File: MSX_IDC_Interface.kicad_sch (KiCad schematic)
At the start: 27 parts, among them J1 DE1 GPIO, J2 Conn_01x03_Male, J3 Conn_01x03_Male, J4 Conn_01x03_Male, J5 Conn_01x03_Male, J6 Conn_01x03_Male, J7 Conn_01x03_Male, Q1 2N2222, Q2 2N2222, U1 74LVC245A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

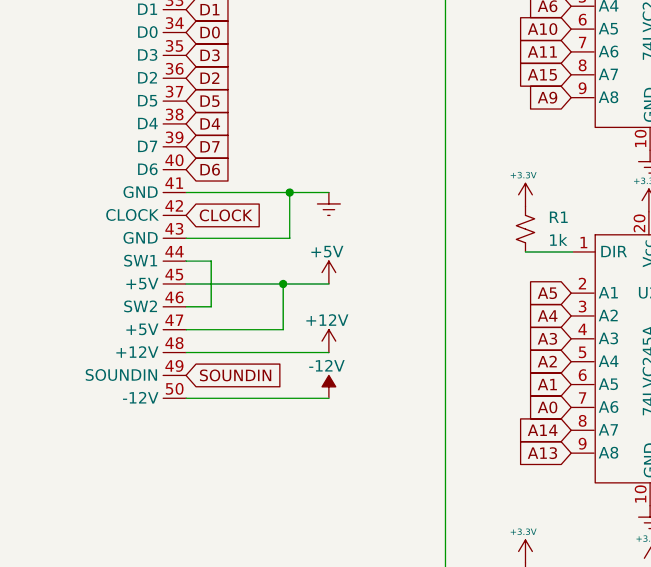
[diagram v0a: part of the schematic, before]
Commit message: Resolvig clearance issues - wip
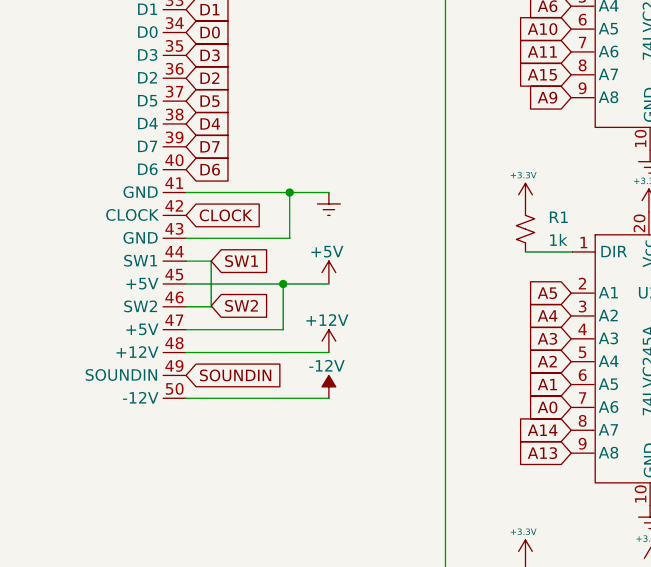
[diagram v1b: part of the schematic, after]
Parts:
- J2, J3, J4, J5, J6, J7: footprint Connector_PinHeader_1.00mm:PinHeader_1x03_P1.00mm_Vertical -> Connector_PinHeader_2.54mm:PinHeader_1x03_P2.54mm_Vertical
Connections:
- net SW1: now reaches CONN1.44 (SW1), CONN1.46 (SW2)
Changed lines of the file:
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@@
+    )
+  )
+  (global_label "SW1" (shape input) (at 35.1862 178.308 0) (fields_autoplaced)
+    (effects (font (size 1.27 1.27)) (justify left))
+    (property "Intersheet References" "${INTERSHEET_REFS}" (id 0) (at 41.4698 178.2286 0)
+      (effects (font (size 1.27 1.27)) (justify left) hide)
     )
   )
@@
     (property "Intersheet References" "${INTERSHEET_REFS}" (id 0) (at 65.6952 65.3574 0)
       (effects (font (size 1.27 1.27)) (justify right) hide)
+    )
+  )
+  (global_label "SW2" (shape input) (at 35.1862 183.2825 0) (fields_autoplaced)
+    (effects (font (size 1.27 1.27)) (justify left))
+    (property "Intersheet References" "${INTERSHEET_REFS}" (id 0) (at 41.4698 183.2031 0)
+      (effects (font (size 1.27 1.27)) (justify left) hide)
     )
   )
@@
   (symbol (lib_id "power:GNDREF") (at 109.5184 219.583 0) (unit 1)
     (in_bom yes) (on_board yes) (fields_autoplaced)
-    (property "Reference" "#PWR?" (id 0) (at 109.5184 225.933 0)
+    (property "Reference" "#PWR0104" (id 0) (at 109.5184 225.933 0)
       (effects (font (size 1.27 1.27)) hide)
     )
@@
   (symbol (lib_id "power:GNDREF") (at 108.204 100.203 0) (unit 1)
     (in_bom yes) (on_board yes) (fields_autoplaced)
-    (property "Reference" "#PWR?" (id 0) (at 108.204 106.553 0)
+    (property "Reference" "#PWR0105" (id 0) (at 108.204 106.553 0)
       (effects (font (size 1.27 1.27)) hide)
     )
@@
   (symbol (lib_id "power:GNDREF") (at 108.204 60.706 0) (unit 1)
     (in_bom yes) (on_board yes) (fields_autoplaced)
-    (property "Reference" "#PWR?" (id 0) (at 108.204 67.056 0)
+    (property "Reference" "#PWR0106" (id 0) (at 108.204 67.056 0)
       (effects (font (size 1.27 1.27)) hide)
     )
@@
       (effects (font (size 1.27 1.27)) hide)
     )
-    (property "Footprint" "Connector_PinHeader_1.00mm:PinHeader_1x03_P1.00mm_Vertical" (id 2) (at 51.816 118.364 0)
+    (property "Footprint" "Connector_PinHeader_2.54mm:PinHeader_1x03_P2.54mm_Vertical" (id 2) (at 51.816 118.364 0)
       (effects (font (size 1.27 1.27)) hide)
     )
@@
       (effects (font (size 1.27 1.27)) hide)
     )
-    (property "Footprint" "Connector_PinHeader_1.00mm:PinHeader_1x03_P1.00mm_Vertical" (id 2) (at 103.124 97.663 0)
+    (property "Footprint" "Connector_PinHeader_2.54mm:PinHeader_1x03_P2.54mm_Vertical" (id 2) (at 103.124 97.663 0)
       (effects (font (size 1.27 1.27)) hide)
     )
@@
       (effects (font (size 1.27 1.27)) hide)
     )
-    (property "Footprint" "Connector_PinHeader_1.00mm:PinHeader_1x03_P1.00mm_Vertical" (id 2) (at 103.124 58.166 0)
+    (property "Footprint" "Connector_PinHeader_2.54mm:PinHeader_1x03_P2.54mm_Vertical" (id 2) (at 103.124 58.166 0)
       (effects (font (size 1.27 1.27)) hide)
     )
@@
   (symbol (lib_id "power:GNDREF") (at 108.847 140.2388 0) (unit 1)
     (in_bom yes) (on_board yes) (fields_autoplaced)
-    (property "Reference" "#PWR?" (id 0) (at 108.847 146.5888 0)
+    (property "Reference" "#PWR0102" (id 0) (at 108.847 146.5888 0)
       (effects (font (size 1.27 1.27)) hide)
     )
@@
       (effects (font (size 1.27 1.27)) hide)
     )
-    (property "Footprint" "Connector_PinHeader_1.00mm:PinHeader_1x03_P1.00mm_Vertical" (id 2) (at 104.2305 177.292 0)
+    (property "Footprint" "Connector_PinHeader_2.54mm:PinHeader_1x03_P2.54mm_Vertical" (id 2) (at 104.2305 177.292 0)
       (effects (font (size 1.27 1.27)) hide)
     )
@@
   (symbol (lib_id "power:GNDREF") (at 109.3105 179.832 0) (unit 1)
     (in_bom yes) (on_board yes) (fields_autoplaced)
-    (property "Reference" "#PWR?" (id 0) (at 109.3105 186.182 0)
+    (property "Reference" "#PWR0103" (id 0) (at 109.3105 186.182 0)
       (effects (font (size 1.27 1.27)) hide)
     )
@@
       (effects (font (size 1.27 1.27)) hide)
     )
-    (property "Footprint" "Connector_PinHeader_1.00mm:PinHeader_1x03_P1.00mm_Vertical" (id 2) (at 103.767 137.6988 0)
+    (property "Footprint" "Connector_PinHeader_2.54mm:PinHeader_1x03_P2.54mm_Vertical" (id 2) (at 103.767 137.6988 0)
       (effects (font (size 1.27 1.27)) hide)
     )
@@
       (effects (font (size 1.27 1.27)) hide)
     )
-    (property "Footprint" "Connector_PinHeader_1.00mm:PinHeader_1x03_P1.00mm_Vertical" (id 2) (at 104.4384 217.043 0)
+    (property "Footprint" "Connector_PinHeader_2.54mm:PinHeader_1x03_P2.54mm_Vertical" (id 2) (at 104.4384 217.043 0)
       (effects (font (size 1.27 1.27)) hide)
     )
@@
       (reference "#PWR0101") (unit 1) (value "GNDREF") (footprint "")
     )
+    (path "/a7f26d93-3fc6-4423-a4ed-f0b3b4593cdf"
+      (reference "#PWR0102") (unit 1) (value "GNDREF") (footprint "")
+    )
+    (path "/c5bbbada-72d1-4e17-b89e-b50fc48d510b"
+      (reference "#PWR0103") (unit 1) (value "GNDREF") (footprint "")
+    )
     (path "/1b971c98-c17e-40e4-bf31-2e4c8421e525"
-      (reference "#PWR?") (unit 1) (value "GNDREF") (footprint "")
+      (reference "#PWR0104") (unit 1) (value "GNDREF") (footprint "")
     )
     (path "/2723d1e6-27f9-43a4-b74d-6d99578b38b4"
-      (reference "#PWR?") (unit 1) (value "GNDREF") (footprint "")
+      (reference "#PWR0105") (unit 1) (value "GNDREF") (footprint "")
     )
     (path "/326dad68-18c6-41b2-abe2-63b86d607d3f"
-      (reference "#PWR?") (unit 1) (value "GNDREF") (footprint "")
-    )
-    (path "/a7f26d93-3fc6-4423-a4ed-f0b3b4593cdf"
-      (reference "#PWR?") (unit 1) (value "GNDREF") (footprint "")
-    )
-    (path "/c5bbbada-72d1-4e17-b89e-b50fc48d510b"
-      (reference "#PWR?") (unit 1) (value "GNDREF") (footprint "")
+      (reference "#PWR0106") (unit 1) (value "GNDREF") (footprint "")
     )
     (path "/d88b88a1-3a49-411f-ab35-844e3052fd45"
@@
     )
     (path "/5c2ceb70-e51a-404f-8c95-a40cc39157b7"
-      (reference "J2") (unit 1) (value "Conn_01x03_Male") (footprint "Connector_PinHeader_1.00mm:PinHeader_1x03_P1.00mm_Vertical")
+      (reference "J2") (unit 1) (value "Conn_01x03_Male") (footprint "Connector_PinHeader_2.54mm:PinHeader_1x03_P2.54mm_Vertical")
     )
     (path "/8ea9f54d-237c-43e0-bfdf-cc3751f268d2"
-      (reference "J3") (unit 1) (value "Conn_01x03_Male") (footprint "Connector_PinHeader_1.00mm:PinHeader_1x03_P1.00mm_Vertical")
+      (reference "J3") (unit 1) (value "Conn_01x03_Male") (footprint "Connector_PinHeader_2.54mm:PinHeader_1x03_P2.54mm_Vertical")
     )
     (path "/784a135c-26c4-4b32-ac75-fe1b2623f928"
-      (reference "J4") (unit 1) (value "Conn_01x03_Male") (footprint "Connector_PinHeader_1.00mm:PinHeader_1x03_P1.00mm_Vertical")
+      (reference "J4") (unit 1) (value "Conn_01x03_Male") (footprint "Connector_PinHeader_2.54mm:PinHeader_1x03_P2.54mm_Vertical")
     )
     (path "/e3bce90c-1784-4929-9ddf-b41e108d9afa"
-      (reference "J5") (unit 1) (value "Conn_01x03_Male") (footprint "Connector_PinHeader_1.00mm:PinHeader_1x03_P1.00mm_Vertical")
+      (reference "J5") (unit 1) (value "Conn_01x03_Male") (footprint "Connector_PinHeader_2.54mm:PinHeader_1x03_P2.54mm_Vertical")
     )
     (path "/bcac35dd-169c-40f7-bf80-ae2250e3d774"
-      (reference "J6") (unit 1) (value "Conn_01x03_Male") (footprint "Connector_PinHeader_1.00mm:PinHeader_1x03_P1.00mm_Vertical")
+      (reference "J6") (unit 1) (value "Conn_01x03_Male") (footprint "Connector_PinHeader_2.54mm:PinHeader_1x03_P2.54mm_Vertical")
     )
     (path "/e8886a90-5ef8-42e8-a3b0-c2e0f5e2d4a1"
-      (reference "J7") (unit 1) (value "Conn_01x03_Male") (footprint "Connector_PinHeader_1.00mm:PinHeader_1x03_P1.00mm_Vertical")
+      (reference "J7") (unit 1) (value "Conn_01x03_Male") (footprint "Connector_PinHeader_2.54mm:PinHeader_1x03_P2.54mm_Vertical")
     )
     (path "/14c2b435-3424-43cf-8040-3e081564fb4f"

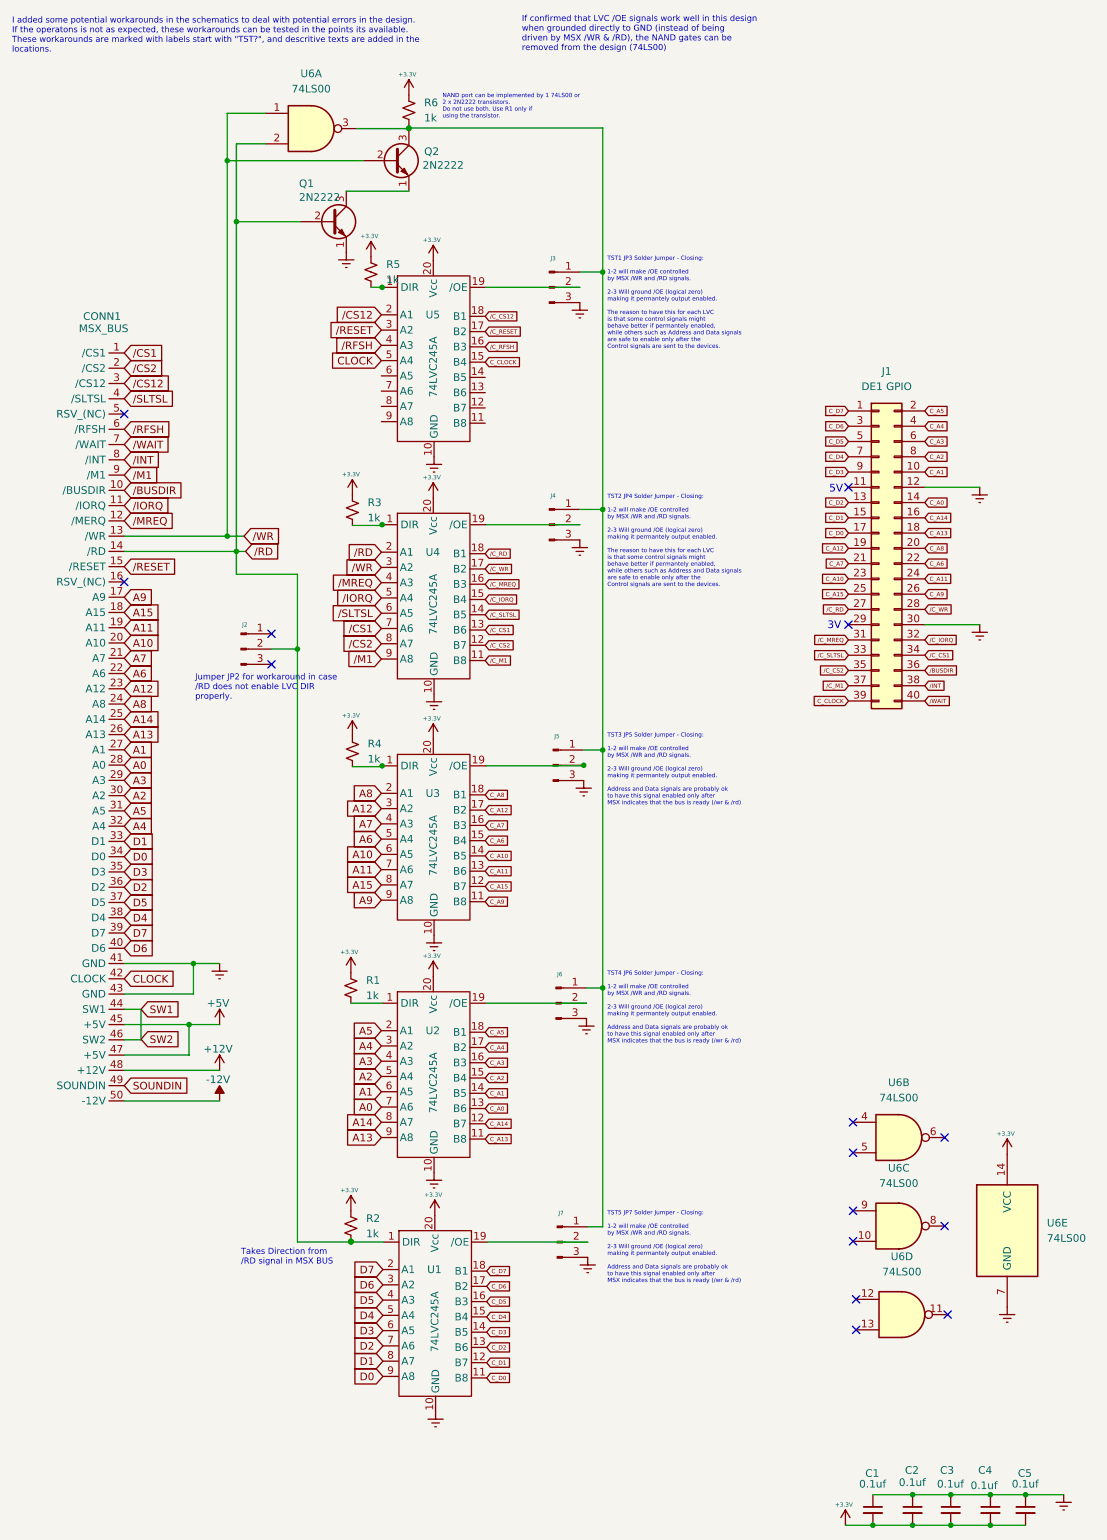
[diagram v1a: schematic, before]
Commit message: Changed NAND gate for XNOR gate (bug); Completed routing
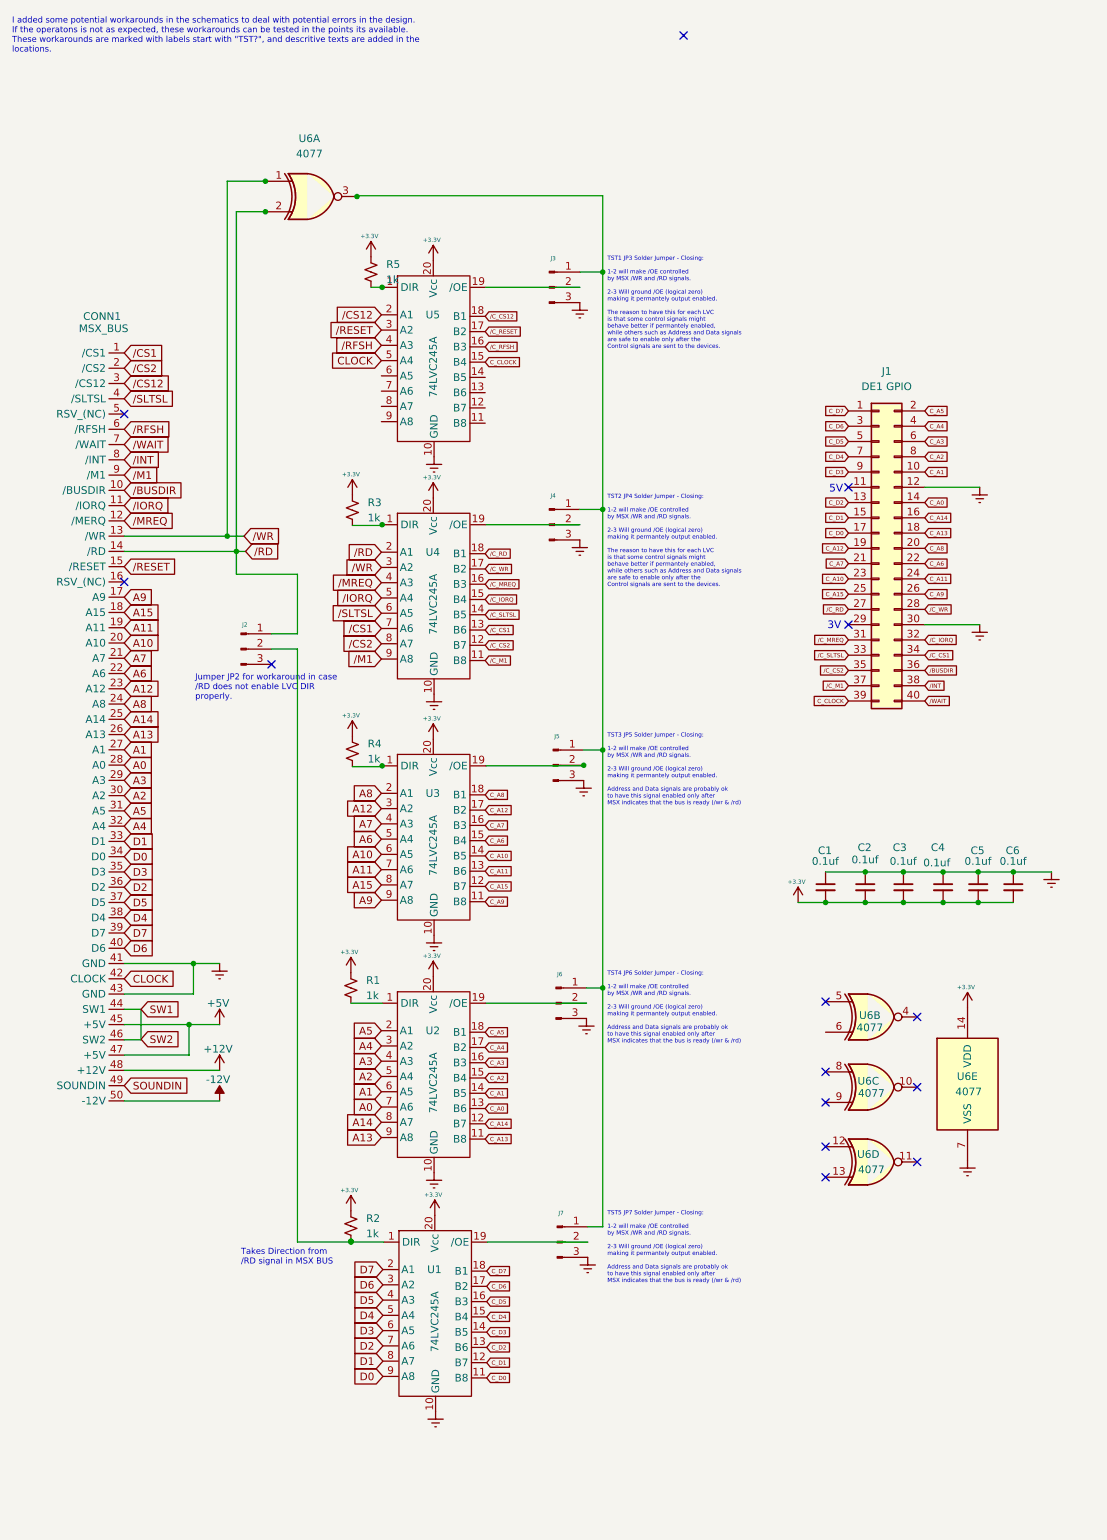
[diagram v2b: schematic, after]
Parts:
- removed Q1, Q2: 2N2222, Roni Footprints:TO127P584H533-3, symbol Transistor_BJT:2N2219
- removed R6: 1k, Resistor_THT:R_Axial_DIN0207_L6.3mm_D2.5mm_P7.62mm_Horizontal, symbol Device:R_Small_US
- removed U6: 74LS00, Package_DIP:DIP-14_W7.62mm, symbol 74xx:74LS00
- added C6: 0.1uf, Capacitor_THT:C_Disc_D3.0mm_W1.6mm_P2.50mm, symbol Device:C_Small
- added U6: 4077, Package_DIP:DIP-14_W7.62mm, symbol 4xxx:4077
- J1: footprint Connector_IDC:IDC-Header_2x20_P2.54mm_Horizontal -> Connector_PinHeader_2.54mm:PinHeader_2x20_P2.54mm_Vertical
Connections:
- net +3.3V: now also C6.2, U6.14 (VDD)
- net GNDREF: now also C6.1, U6.7 (VSS)
- net /RD: now also J2.1 (Pin_1), U6.2; no longer J2.2 (Pin_2), R2.2, U1.1 (DIR)
- net /WR: now also U6.1
- net at J3.1 (Pin_1), J4.1 (Pin_1), J5.1 (Pin_1)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: now also U6.3
- new net: J2.2 (Pin_2), R2.2, U1.1 (DIR)
- no-connect marks 15 -> 14
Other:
- note removed: "If confirmed that LVC /OE signals work well in this design when grounded directly to GND (instead of being driven by MSX /WR & /RD), the NAND gates can be removed from the design (74LS00)"
- note removed: "NAND port can be implemented by 1 74LS00 or 2 x 2N2222 transistors. Do not use both. Use R1 only if using the transistor."
- moved on the sheet: C1, C2, C3, C4, C5
